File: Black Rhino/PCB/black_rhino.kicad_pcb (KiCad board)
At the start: 2 copper layers, 266.7 x 113.5 mm, 150 parts, among them SW1 SW_Push, U1 ATmega32U4-AU, Y1 16MHz

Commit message: Wire Black-Rhino-PCB
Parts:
- moved C5 3.66 mm to (158.1, 61.1), turned to 0 degrees
- moved U1 1.40 mm to (149.1, 54.0)
- moved C6 0.34 mm to (136.3, 57.7), turned to 90 degrees
- moved R4 0.34 mm to (137.1, 60.8)
- moved C3 0.19 mm to (136.2, 47.0)
- moved C7 0.19 mm to (136.2, 50.2)
- moved R1 0.16 mm to (165.0, 46.9)
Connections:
- U1 pad 10: NONE -> Net-(U1-Pad10)
- U1 pad 11: NONE -> Net-(U1-Pad11)
- U1 pad 12: NONE -> Net-(U1-Pad12)
- U1 pad 8: NONE -> Net-(U1-Pad8)
- U1 pad 9: NONE -> Net-(U1-Pad9)
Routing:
- net ROW4: track 0.00 -> 474.1 mm
- net ROW3: track 0.00 -> 454.3 mm
- net ROW2: track 0.00 -> 433.8 mm
- net ROW1: track 0.00 -> 433.0 mm
- net ROW0: track 0.00 -> 394.9 mm
- net GND: track 0.00 -> 215.0 mm, vias 0 -> 2
- net +5V: track 0.00 -> 208.6 mm, vias 0 -> 4
- net COL0: track 0.00 -> 206.2 mm
- net COL13: track 0.00 -> 199.7 mm
- net COL1: track 0.00 -> 184.7 mm
- net COL12: track 0.00 -> 181.8 mm
- net COL2: track 0.00 -> 167.3 mm
- net COL11: track 0.00 -> 163.2 mm
- net COL3: track 0.00 -> 148.3 mm
- net COL10: track 0.00 -> 145.2 mm
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- added copper zone on B.Cu, net GND
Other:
- board size 266.7 x 113.5 mm -> 271.5 x 113.5 mm
- net class Default: trace_width 0.25 -> 0.254
- net class Power added: clearance 0.2, trace_width 0.381, via_dia 0.8, via_drill 0.4
- board text added: "Diceros Bicornis"

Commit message: Improve Black-Rhino-PCB & Add MountingHoles
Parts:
- added H1: MountingHole, MountingHole:MountingHole_2mm, B.Cu at (16.7, 49.2)
- added H10: MountingHole, MountingHole:MountingHole_2mm, B.Cu at (16.7, 59.5)
- added H11: MountingHole, MountingHole:MountingHole_2mm, B.Cu at (119.9, 59.5)
- added H12: MountingHole, MountingHole:MountingHole_2mm, B.Cu at (119.9, 49.2)
- added H13: MountingHole, MountingHole:MountingHole_2mm, B.Cu at (53.2, 119.9)
- added H14: MountingHole, MountingHole:MountingHole_2mm, B.Cu at (34.1, 81.8)
- added H15: MountingHole, MountingHole:MountingHole_2mm, B.Cu at (243.7, 119.9)
- added H16: MountingHole, MountingHole:MountingHole_2mm, B.Cu at (262.7, 81.8)
- added H17: MountingHole, MountingHole:MountingHole_2mm, B.Cu at (148.4, 138.9)
- added H18: MountingHole, MountingHole:MountingHole_2mm, B.Cu at (148.4, 81.8)
- added H19: MountingHole, MountingHole:MountingHole_2mm, B.Cu at (111.9, 49.2)
- added H2: MountingHole, MountingHole:MountingHole_2mm, B.Cu at (280.2, 48.4)
- added H20: MountingHole, MountingHole:MountingHole_2mm, B.Cu at (111.9, 59.5)
- added H21: MountingHole, MountingHole:MountingHole_2mm, B.Cu at (16.7, 67.5)
- added H3: MountingHole, MountingHole:MountingHole_2mm, B.Cu at (280.2, 154.0)
- added H4: MountingHole, MountingHole:MountingHole_2mm, B.Cu at (16.7, 154.0)
- added H5: MountingHole, MountingHole:MountingHole_2mm, B.Cu at (91.3, 81.8)
- added H6: MountingHole, MountingHole:MountingHole_2mm, B.Cu at (205.6, 81.8)
- added H7: MountingHole, MountingHole:MountingHole_2mm, B.Cu at (205.6, 138.9)
- added H8: MountingHole, MountingHole:MountingHole_2mm, B.Cu at (91.3, 138.9)
- added H9: MountingHole, MountingHole:MountingHole_2mm, B.Cu at (111.9, 67.5)
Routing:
- net COL4: track 114.9 -> 110.1 mm
- net +5V: track 208.6 -> 210.2 mm
- net ROW4: track 474.1 -> 474.7 mm
- net ROW1: track 433.0 -> 433.6 mm
- net ROW0: track 394.9 -> 395.5 mm
- net ROW3: track 454.3 -> 454.9 mm
- net ROW2: track 433.8 -> 434.4 mm

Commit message: Fix Black Rhino-PCB & -MountingHoles
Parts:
- added H22: MountingHole, MountingHole:MountingHole_2mm, B.Cu at (205.6, 48.4)
- moved H5 19.1 mm to (91.3, 100.8)
- moved H6 19.1 mm to (205.6, 100.8)
- moved H1 0.79 mm to (16.7, 48.4)
- moved H12 0.79 mm to (119.9, 48.4)
- moved H19 0.79 mm to (111.9, 48.4)
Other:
- outline, holes or cut-outs redrawn
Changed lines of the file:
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@@
     (tracks 920)
     (zones 0)
-    (modules 171)
+    (modules 172)
     (nets 108)
   )
@@
     (add_net GND)
   )
+  (module MountingHole:MountingHole_2mm (layer B.Cu)
+    (at 205.58125 48.41875)
+    (descr "Mounting Hole 2mm, no annular")
+    (tags "mounting hole 2mm no annular")
+    (attr virtual)
+    (fp_text reference H22 (at 0 3.2) (layer B.SilkS)
+      (effects (font (size 1 1) (thickness 0.15)) (justify mirror))
+    )
+    (fp_text value MountingHole (at 0 -3.1) (layer B.Fab)
+      (effects (font (size 1 1) (thickness 0.15)) (justify mirror))
+    )
+    (fp_circle (center 0 0) (end 2.25 0) (layer B.CrtYd) (width 0.05))
+    (fp_circle (center 0 0) (end 2 0) (layer Cmts.User) (width 0.15))
+    (fp_text user %R (at 0.3 0) (layer B.Fab)
+      (effects (font (size 1 1) (thickness 0.15)) (justify mirror))
+    )
+    (pad "" np_thru_hole circle (at 0 0) (size 2 2) (drill 2) (layers *.Cu *.Mask))
+  )
   (module MX_Alps_Hybrid:MX-1U (layer F.Cu)
     (at 272.25625 72.23125)
@@
   )
   (module MountingHole:MountingHole_2mm (layer B.Cu)
-    (at 111.91875 49.2125)
+    (at 111.91875 48.41875)
     (descr "Mounting Hole 2mm, no annular")
     (tags "mounting hole 2mm no annular")
@@
   )
   (module MountingHole:MountingHole_2mm (layer B.Cu)
-    (at 119.85625 49.2125)
+    (at 119.85625 48.41875)
     (descr "Mounting Hole 2mm, no annular")
     (tags "mounting hole 2mm no annular")
@@
   )
   (module MountingHole:MountingHole_2mm (layer B.Cu)
-    (at 205.58125 81.75625)
+    (at 205.58125 100.80625)
     (descr "Mounting Hole 2mm, no annular")
     (tags "mounting hole 2mm no annular")
@@
   )
   (module MountingHole:MountingHole_2mm (layer B.Cu)
-    (at 91.28125 81.75625)
+    (at 91.28125 100.80625)
     (descr "Mounting Hole 2mm, no annular")
     (tags "mounting hole 2mm no annular")
@@
   )
   (module MountingHole:MountingHole_2mm (layer B.Cu)
-    (at 16.66875 49.2125)
+    (at 16.66875 48.41875)
     (descr "Mounting Hole 2mm, no annular")
     (tags "mounting hole 2mm no annular")
@@
     (effects (font (size 5 5) (thickness 0.45)))
   )
-  (gr_line (start 280.9875 44.45) (end 15.08125 45.24375) (layer Edge.Cuts) (width 0.05))
+  (gr_line (start 280.9875 44.45) (end 15.08125 44.45) (layer Edge.Cuts) (width 0.05))
   (gr_arc (start 280.9875 47.625) (end 284.1625 47.625) (angle -90) (layer Edge.Cuts) (width 0.05))
-  (gr_arc (start 15.08125 47.625) (end 15.08125 45.24375) (angle -90) (layer Edge.Cuts) (width 0.05))
-  (gr_line (start 12.7 47.625) (end 12.7 155.575) (layer Edge.Cuts) (width 0.05))
+  (gr_arc (start 15.08125 46.83125) (end 15.08125 44.45) (angle -90) (layer Edge.Cuts) (width 0.05))
+  (gr_line (start 12.7 46.83125) (end 12.7 155.575) (layer Edge.Cuts) (width 0.05))
   (gr_line (start 284.1625 155.575) (end 284.1625 47.625) (layer Edge.Cuts) (width 0.05))
   (gr_line (start 15.08125 157.95625) (end 281.78125 157.95625) (layer Edge.Cuts) (width 0.05))

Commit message: Change Black Rhino-PCB & Change Amur Leopard Libs
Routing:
- net +5V: track 210.2 -> 182.7 mm
- net Net-(C2-Pad2): track 39.8 -> 36.1 mm
- net GND: track 215.0 -> 216.8 mm, vias 2 -> 0

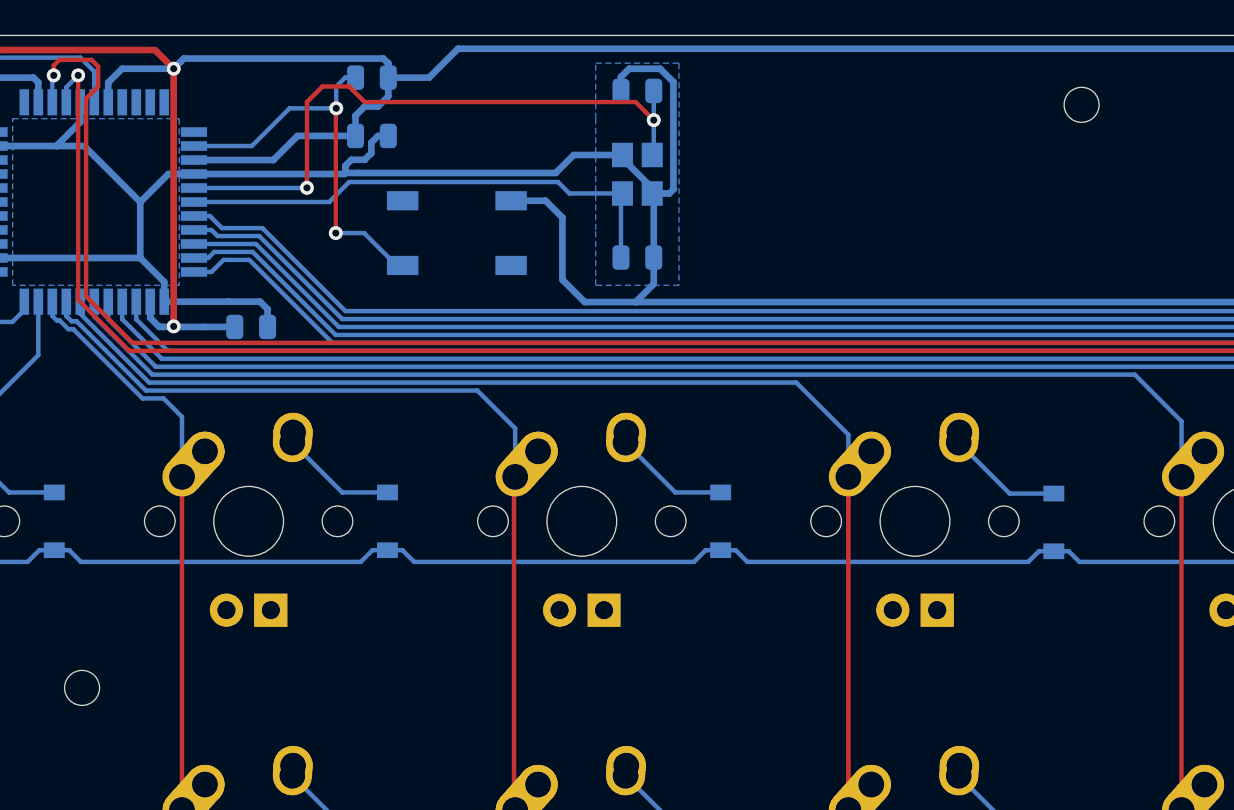
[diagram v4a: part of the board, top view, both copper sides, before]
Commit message: Add Indicator-LEDs to Black Rhino
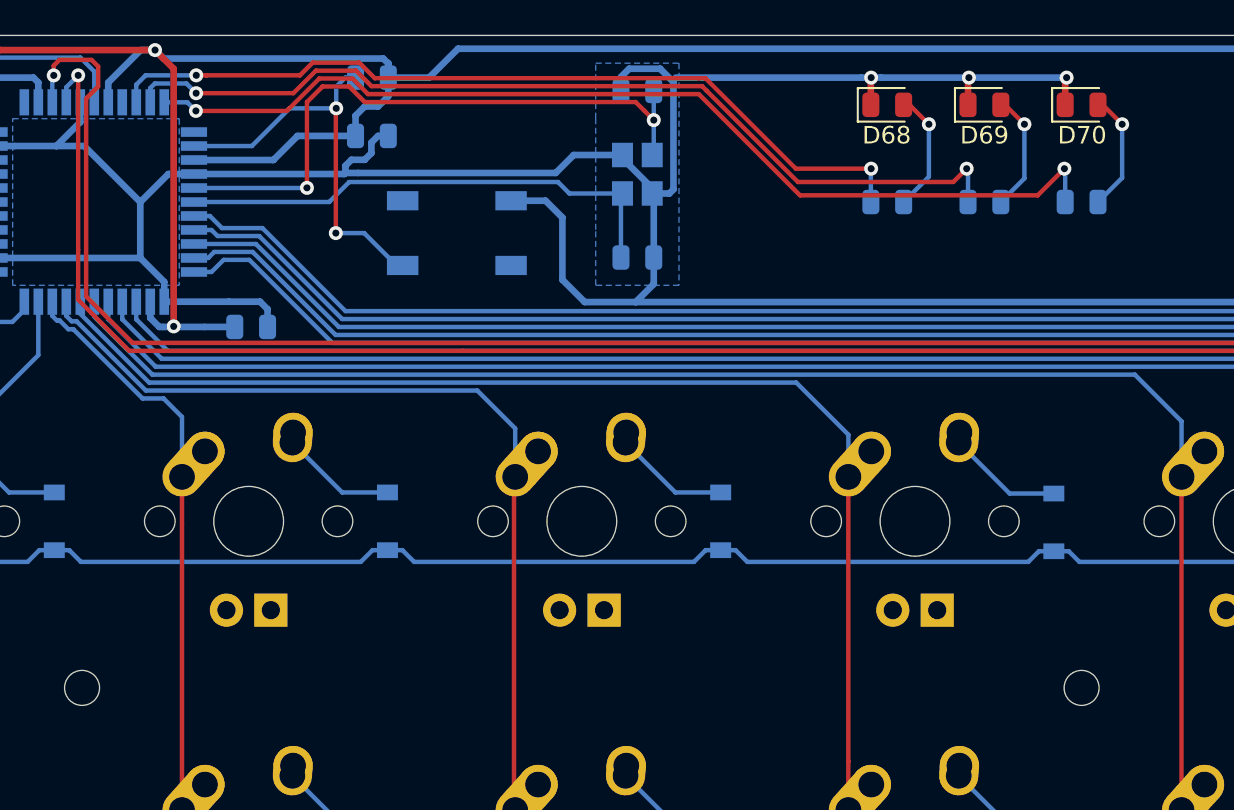
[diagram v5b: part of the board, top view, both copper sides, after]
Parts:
- added D68: LED, LED_SMD:LED_0805_2012Metric, F.Cu at (194.5, 48.4)
- added D69: LED, LED_SMD:LED_0805_2012Metric, F.Cu at (200.0, 48.4)
- added D70: LED, LED_SMD:LED_0805_2012Metric, F.Cu at (205.6, 48.4)
- added R5: R_Small, Resistor_SMD:R_0805_2012Metric, B.Cu at (194.5, 54.0)
- added R6: R_Small, Resistor_SMD:R_0805_2012Metric, B.Cu at (200.0, 54.0)
- added R7: R_Small, Resistor_SMD:R_0805_2012Metric, B.Cu at (205.6, 54.0)
- moved H22 33.3 mm to (205.6, 81.8)
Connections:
- U1 pad 10: Net-(U1-Pad10) -> LED1
- U1 pad 11: Net-(U1-Pad11) -> LED2
- U1 pad 9: Net-(U1-Pad9) -> LED0
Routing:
- net LED2: track 0.00 -> 57.8 mm, vias 0 -> 2
- net LED1: track 0.00 -> 53.3 mm, vias 0 -> 2
- net LED0: track 0.00 -> 48.0 mm, vias 0 -> 2
- net GND: track 216.8 -> 243.9 mm, vias 0 -> 3
- net Net-(D68-Pad2): track 0.00 -> 6.92 mm, vias 0 -> 1
- net Net-(D70-Pad2): track 0.00 -> 6.86 mm, vias 0 -> 1
- net Net-(D69-Pad2): track 0.00 -> 6.81 mm, vias 0 -> 1

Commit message: Add Ohms to LED-Resistors of Black Rhino
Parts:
- R5, R6, R7: value R_Small -> 470
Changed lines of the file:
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@@
     (tags resistor)
     (attr smd)
-    (fp_text reference R7 (at 0 1.65) (layer B.SilkS)
+    (fp_text reference R7 (at -0.79375 1.651) (layer B.SilkS)
       (effects (font (size 1 1) (thickness 0.15)) (justify mirror))
     )
-    (fp_text value R_Small (at 0 -1.65) (layer B.Fab)
+    (fp_text value 470 (at 0 -1.65) (layer B.Fab)
       (effects (font (size 1 1) (thickness 0.15)) (justify mirror))
     )
@@
     (tags resistor)
     (attr smd)
-    (fp_text reference R6 (at 0 1.65) (layer B.SilkS)
+    (fp_text reference R6 (at -0.762 1.651) (layer B.SilkS)
       (effects (font (size 1 1) (thickness 0.15)) (justify mirror))
     )
-    (fp_text value R_Small (at 0 -1.65) (layer B.Fab)
+    (fp_text value 470 (at 0 -1.65) (layer B.Fab)
       (effects (font (size 1 1) (thickness 0.15)) (justify mirror))
     )
@@
     (tags resistor)
     (attr smd)
-    (fp_text reference R5 (at 0 1.65) (layer B.SilkS)
+    (fp_text reference R5 (at -0.73025 1.65) (layer B.SilkS)
       (effects (font (size 1 1) (thickness 0.15)) (justify mirror))
     )
-    (fp_text value R_Small (at 0 -1.65) (layer B.Fab)
+    (fp_text value 470 (at 0 -1.65) (layer B.Fab)
       (effects (font (size 1 1) (thickness 0.15)) (justify mirror))
     )

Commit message: Fix Black Rhino-PCB
I only needed 1 Indicator-LED and added 3 in commit:
67b9c5aa973747f4bc26af49aa7426545263447c
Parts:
- removed D69, D70: LED, LED_SMD:LED_0805_2012Metric
- removed R6, R7: 470, Resistor_SMD:R_0805_2012Metric
- MX28, MX60, MX61: footprint MX_Alps_Hybrid:MX-1U -> MX_Alps_Hybrid:MX-2U
- moved D41 6.35 mm to (261.1, 116.7)
- moved D27 6.35 mm to (261.1, 97.6)
- moved D68 5.56 mm to (200.0, 48.4)
- moved R5 5.56 mm to (200.0, 54.0)
- moved D28 0.79 mm to (281.0, 100.8)
- turned MX28 to 90 degrees
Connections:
- U1 pad 10: LED1 -> Net-(U1-Pad10)
- U1 pad 11: LED2 -> LED0
- U1 pad 9: LED0 -> Net-(U1-Pad9)
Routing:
- net LED2: track 57.8 -> 0.00 mm, vias 2 -> 0
- net LED1: track 53.3 -> 0.00 mm, vias 2 -> 0
- net GND: track 243.9 -> 209.7 mm
- net ROW2: track 434.4 -> 444.5 mm
- net Net-(D28-Pad2): track 6.62 -> 15.3 mm
- net ROW1: track 433.6 -> 441.8 mm
- net Net-(D70-Pad2): track 6.86 -> 0.00 mm, vias 1 -> 0
- net Net-(D69-Pad2): track 6.81 -> 0.00 mm, vias 1 -> 0
- net Net-(D41-Pad2): track 6.62 -> 13.2 mm
- net Net-(D27-Pad2): track 6.62 -> 12.9 mm
- net LED0: track 48.0 -> 51.6 mm
- net ROW3: track 454.9 -> 456.2 mm
- net ROW0: track 395.5 -> 396.7 mm
- net ROW4: track 474.7 -> 475.9 mm
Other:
- board size 271.5 x 113.5 mm -> 271.5 x 115.9 mm
- board text added: "CAPS"

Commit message: Improve Black Rhino-PCB
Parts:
- moved C1 16.0 mm to (164.2, 57.3)
- moved C2 16.0 mm to (164.2, 47.8)
- moved Y1 16.0 mm to (164.2, 52.5)
- moved SW1 12.4 mm to (181.8, 52.4)
- moved C4 7.05 mm to (158.0, 50.0)
- moved R1 7.05 mm to (158.0, 46.8)
- moved C6 4.33 mm to (140.5, 58.7), turned to 180 degrees
- moved C3 4.26 mm to (140.5, 46.8)
- moved C7 4.26 mm to (140.5, 50.0), turned to 180 degrees
- moved F1 3.78 mm to (244.4, 54.8)
- moved R4 3.56 mm to (140.5, 61.9)
- moved C5 1.31 mm to (157.2, 60.2), turned to 90 degrees
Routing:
- net Net-(C2-Pad2): track 36.1 -> 16.1 mm, vias 2 -> 0
- net GND: track 209.7 -> 191.0 mm, vias 3 -> 1
- net Net-(R1-Pad2): track 23.3 -> 40.9 mm
- net Net-(C1-Pad2): track 28.9 -> 12.3 mm
- net +5V: track 183.1 -> 170.5 mm
- net Net-(C3-Pad1): track 15.1 -> 10.7 mm
- net Net-(R4-Pad2): track 7.85 -> 5.03 mm
- net COL6: track 98.6 -> 97.0 mm
- net ROW4: track 475.9 -> 477.0 mm
- net ROW3: track 456.2 -> 457.2 mm
- net ROW2: track 444.5 -> 445.5 mm
- net COL7: track 71.2 -> 70.2 mm
- net COL12: track 181.8 -> 180.9 mm
- net COL11: track 163.2 -> 162.3 mm
- net COL5: track 114.5 -> 113.7 mm
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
